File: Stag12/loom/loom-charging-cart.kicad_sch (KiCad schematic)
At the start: 47 parts, among them J1 523-2CMA193122R1000, J2 Conn_01x08_Pin, J38 Conn_01x04_Pin, J39 Conn_01x04_Pin, J40 Conn_01x08_Pin, J41 TSAL, J42 LATCHING, J43 POWER, J44 LATCHING, J45 Conn_01x02_Pin, J46 Conn_01x02_Pin, J47 Conn_01x02_Pin, J48 Conn_01x02_Pin, J49 Conn_01x02_Pin, J50 Conn_01x02_Pin, J51 Conn_01x02_Pin, J52 523-2CMA193122R1000, K1 Relay_DPST-NO, K2 Relay_DPST-NO, SW1 E-Stop, SW11 SW_DPST, SW14 SW_DPST, SW15 Close AIRs, SW16 Latching Reset, SW17 E-Stop, SW18 SW_DPST, SW19 SW_DPST, SW2 Latching Reset, SW3 Close AIRs

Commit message: forgot to save
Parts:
- added CB1: RS PRO DHMZ, symbol Device:CircuitBreaker_1P
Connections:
- net MAINS_L_IN: now also CB1.2; no longer K2.23, SW19.1
- new net: CB1.1, K2.23, SW19.1
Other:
- moved on the sheet: SW19
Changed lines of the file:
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@@
 	)
 	(junction
-		(at 22.86 246.38)
-		(diameter 0)
-		(color 0 0 0 0)
-	)
-	(junction
 		(at 71.12 83.82)
 		(diameter 0)
@@
 	)
 	(junction
-		(at 25.4 243.84)
-		(diameter 0)
-		(color 0 0 0 0)
-	)
-	(junction
 		(at 217.17 132.08)
 		(diameter 0)
@@
 	)
 	(junction
+		(at 44.45 246.38)
+		(diameter 0)
+		(color 0 0 0 0)
+	)
+	(junction
 		(at 71.12 81.28)
 		(diameter 0)
@@
 	)
 	(junction
+		(at 46.99 243.84)
+		(diameter 0)
+		(color 0 0 0 0)
+	)
+	(junction
 		(at 99.06 93.98)
 		(diameter 0)
@@
 	(wire
 		(pts
-			(xy 22.86 246.38) (xy 22.86 265.43)
-		)
-		(stroke
-			(width 0)
-			(type default)
-		)
-	)
-	(wire
-		(pts
-			(xy 22.86 246.38) (xy 127 246.38)
-		)
-		(stroke
-			(width 0)
-			(type default)
-		)
-	)
-	(wire
-		(pts
 			(xy 205.74 59.69) (xy 205.74 35.56)
 		)
@@
 	(wire
 		(pts
-			(xy 36.195 260.35) (xy 25.4 260.35)
+			(xy 57.785 260.35) (xy 46.99 260.35)
 		)
 		(stroke
@@
 	(wire
 		(pts
+			(xy 44.45 246.38) (xy 44.45 265.43)
+		)
+		(stroke
+			(width 0)
+			(type default)
+		)
+	)
+	(wire
+		(pts
 			(xy 161.29 419.1) (xy 161.29 406.4)
 		)
@@
 	(wire
 		(pts
-			(xy 25.4 260.35) (xy 25.4 243.84)
-		)
-		(stroke
-			(width 0)
-			(type default)
-		)
-	)
-	(wire
-		(pts
 			(xy 19.05 230.505) (xy 19.05 248.92)
 		)
@@
 	(wire
 		(pts
-			(xy 3.175 243.84) (xy 25.4 243.84)
+			(xy 3.175 243.84) (xy 23.495 243.84)
 		)
 		(stroke
@@
 	(wire
 		(pts
-			(xy 46.355 260.35) (xy 75.565 260.35)
+			(xy 67.945 260.35) (xy 75.565 260.35)
 		)
 		(stroke
@@
 	(wire
 		(pts
-			(xy 25.4 243.84) (xy 127.635 243.84)
-		)
-		(stroke
-			(width 0)
-			(type default)
-		)
-	)
-	(wire
-		(pts
 			(xy 19.05 230.505) (xy 43.815 230.505)
 		)
@@
 	(wire
 		(pts
+			(xy 38.735 243.84) (xy 46.99 243.84)
+		)
+		(stroke
+			(width 0)
+			(type default)
+		)
+	)
+	(wire
+		(pts
 			(xy 158.75 408.94) (xy 158.75 406.4)
 		)
@@
 	(wire
 		(pts
-			(xy 46.355 265.43) (xy 75.565 265.43)
+			(xy 67.945 265.43) (xy 75.565 265.43)
 		)
 		(stroke
@@
 	(wire
 		(pts
+			(xy 46.99 243.84) (xy 46.99 260.35)
+		)
+		(stroke
+			(width 0)
+			(type default)
+		)
+	)
+	(wire
+		(pts
 			(xy 180.34 59.69) (xy 175.26 59.69)
 		)
@@
 	(wire
 		(pts
-			(xy 22.86 265.43) (xy 36.195 265.43)
+			(xy 44.45 265.43) (xy 57.785 265.43)
 		)
 		(stroke
@@
 	(wire
 		(pts
+			(xy 44.45 246.38) (xy 127 246.38)
+		)
+		(stroke
+			(width 0)
+			(type default)
+		)
+	)
+	(wire
+		(pts
 			(xy 73.025 292.735) (xy 99.695 292.735)
 		)
@@
 	(wire
 		(pts
+			(xy 46.99 243.84) (xy 127.635 243.84)
+		)
+		(stroke
+			(width 0)
+			(type default)
+		)
+	)
+	(wire
+		(pts
 			(xy 217.17 132.08) (xy 217.17 151.13)
 		)
@@
 	(wire
 		(pts
-			(xy 3.175 246.38) (xy 22.86 246.38)
+			(xy 3.175 246.38) (xy 44.45 246.38)
 		)
 		(stroke
@@
 	(symbol
 		(lib_id "Switch:SW_DPST")
-		(at 41.275 262.89 0)
+		(at 62.865 262.89 0)
 		(mirror x)
 		(unit 1)
@@
 		(dnp no)
 		(property "Reference" "SW19"
-			(at 43.815 268.605 0)
+			(at 65.405 268.605 0)
 			(effects
 				(font
@@
 		)
 		(property "Value" "SW_DPST"
-			(at 45.72 257.175 0)
+			(at 67.31 257.175 0)
 			(effects
 				(font
@@
 		)
 		(property "Footprint" ""
-			(at 41.275 262.89 0)
+			(at 62.865 262.89 0)
 			(effects
 				(font
@@
 		)
 		(property "Datasheet" "~"
-			(at 41.275 262.89 0)
+			(at 62.865 262.89 0)
 			(effects
 				(font
@@
 		)
 		(property "Description" "Double Pole Single Throw (DPST) Switch"
-			(at 41.275 262.89 0)
+			(at 62.865 262.89 0)
 			(effects
 				(font
@@
 					(unit 1)
 				)
+			)
+		)
+	)
+	(symbol
+		(lib_id "Device:CircuitBreaker_1P")
+		(at 31.115 243.84 270)
+		(unit 1)
+		(exclude_from_sim no)
+		(in_bom yes)
+		(on_board yes)
+		(dnp no)
+		(fields_autoplaced yes)
+		(property "Reference" "CB1"
+			(at 31.115 236.22 90)
+			(effects
+				(font
+					(size 1.27 1.27)
+				)
+			)
+		)
+		(property "Value" "RS PRO DHMZ"
+			(at 31.115 238.76 90)
+			(effects
+				(font
+					(size 1.27 1.27)
+				)
+			)
+		)
+		(property "Footprint" ""
+			(at 31.115 243.84 0)
+			(effects
+				(font
+					(size 1.27 1.27)
+				)
+				(hide yes)
+			)
+		)
+		(property "Datasheet" "~"
+			(at 31.115 243.84 0)
+			(effects
+				(font
+					(size 1.27 1.27)
+				)
+				(hide yes)
+			)
+		)
+		(property "Description" "Single pole circuit breaker"
+			(at 31.115 243.84 0)
+			(effects
+				(font
+					(size 1.27 1.27)
+				)
+				(hide yes)
+			)
+		)
+		(pin "1"
+		)
+		(pin "2"
+		)
+		(instances
+			(project ""
+				(path "/03011643-0690-4b85-ab78-d6a62dae52b1/c24e4324-79c1-4828-a7be-e83d495a6b6b"
+					(reference "CB1")
+					(unit 1)
+				)

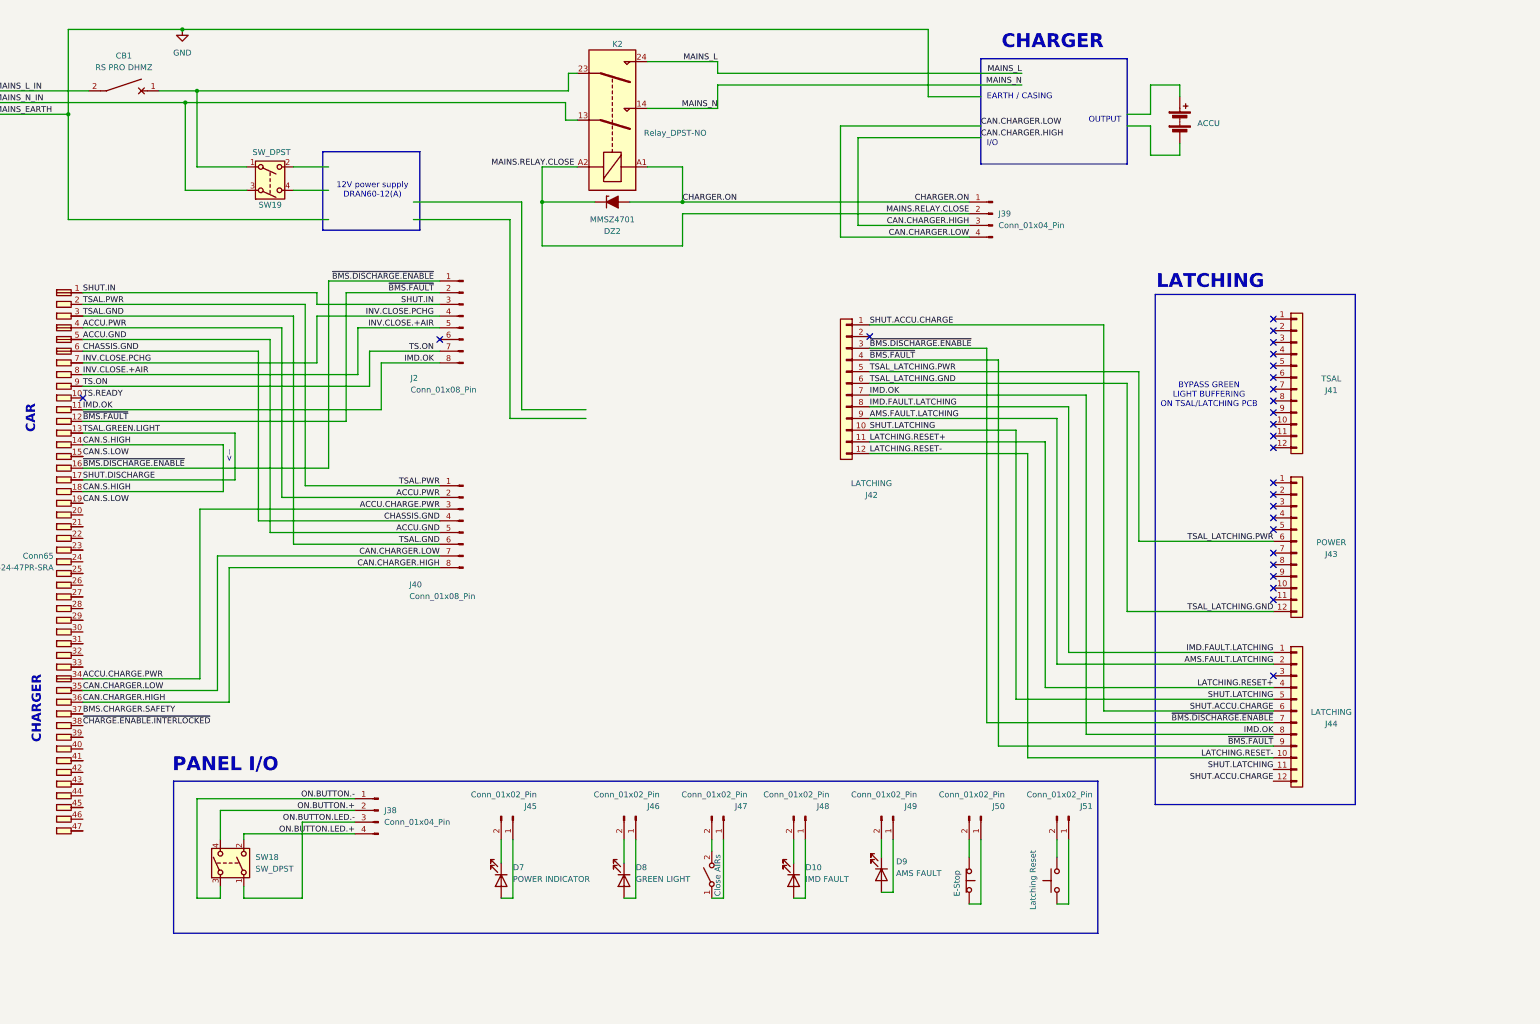
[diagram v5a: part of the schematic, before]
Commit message: Update loom-charging-cart.kicad_sch
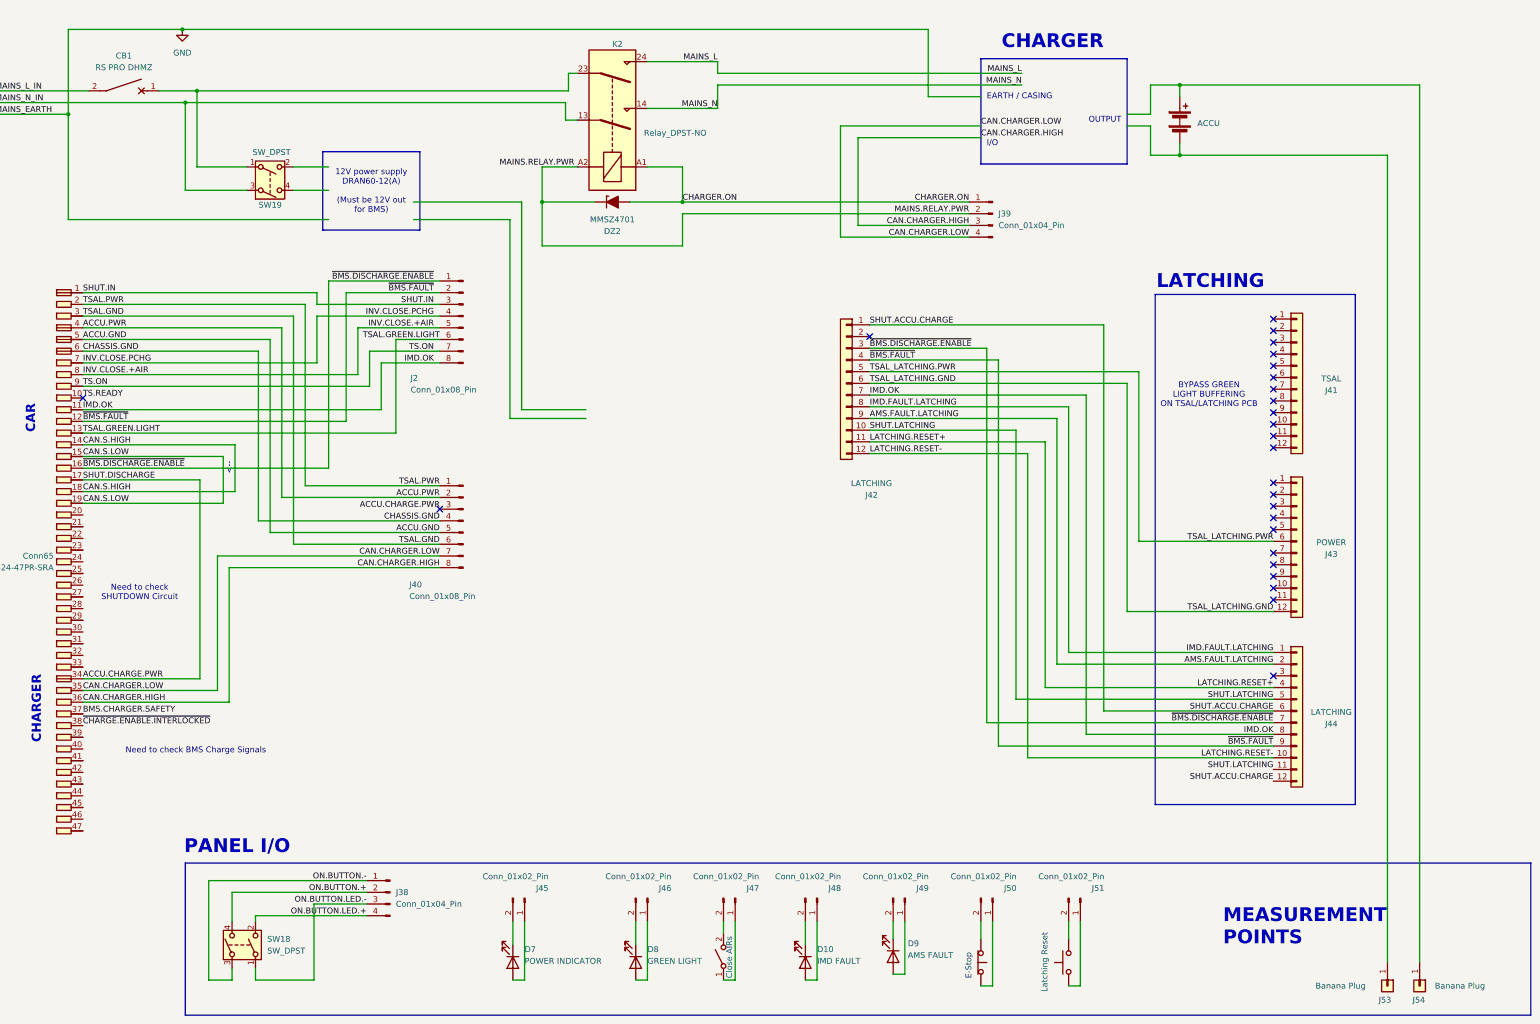
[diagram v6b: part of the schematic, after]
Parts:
- added J53, J54: Banana Plug, symbol Connector_Generic:Conn_01x01
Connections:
- net +12V: now also Conn57.17, Conn65.17
- net TSAL.GREEN.LIGHT: now reaches J2.6 (Pin_6)
- net TSAL.GREEN.LIGHT: now also Conn57.13, Conn65.13
- net at BT2.1 (+): now also J54.1 (Pin_1)
- net at BT2.2 (-): now also J53.1 (Pin_1)
- net MAINS.RELAY.CLOSE renamed MAINS.RELAY.PWR
- removed net SHUT.DISCHARGE: Conn57.13, Conn57.17, Conn65.13, Conn65.17
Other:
- note added: "12V power supply DRAN60-12(A) (Must be 12V out for BMS)"
- note added: "MEASUREMENT POINTS"
- note added: "Need to check BMS Charge Signals"
- note added: "Need to check SHUTDOWN Circuit"
- note removed: "12V power supply DRAN60-12(A)"
- moved on the sheet: D10, D7, D8, D9, J38, J45, J46, J47, J48, J49, J50, J51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
